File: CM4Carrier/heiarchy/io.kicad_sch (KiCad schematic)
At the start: 3 parts

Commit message: wiring some stuff
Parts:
- added C?: 10u, Capacitor_SMD:C_0805_2012Metric, symbol Device:C
- added D?: (no value), symbol Device:LED
- added R? (x2): (no value), symbol Device:R
- added TP?: (no value), symbol Connector:TestPoint_Flag
- added TP?: (no value), symbol Connector:TestPoint
- added U?: (no value), symbol Power_Management:MIC2025-2YMM
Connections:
- net GND: now also J?.6 (VSS), C?.2, U?.3 (GND)
- net IO_VREF: now also D?.2 (A), R?.2, TP?.1, U?.7 (IN)
- net SD_CMD: now reaches J?.3 (CMD)
- net SD_CMD: now also Module1.62 (SD_CMD)
- net SD_PWR: now reaches J?.4 (VDD)
- net SD_PWR: now also C?.1, U?.6 (OUT), U?.8 (OUT)
- net SD_CLK: now reaches J?.5 (CLK)
- net SD_CLK: now also Module1.57 (SD_CLK)
- net at Module1.21 (PI_nLED_Activity): now also R?.2
- net SD_PWR_ON: now reaches Module1.75 (SD_PWR_ON)
- net SD_PWR_ON: now also R?.1, U?.1 (EN)
- net at Module1.95 (nPI_LED_PWR): now also TP?.1
- new net: D?.1 (K), R?.1
- no-connect marks 0 -> 7
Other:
- note added: "SD CARD"
- note added: "if an sd card is overcurrent... what?"
- moved on the sheet: J?, R?

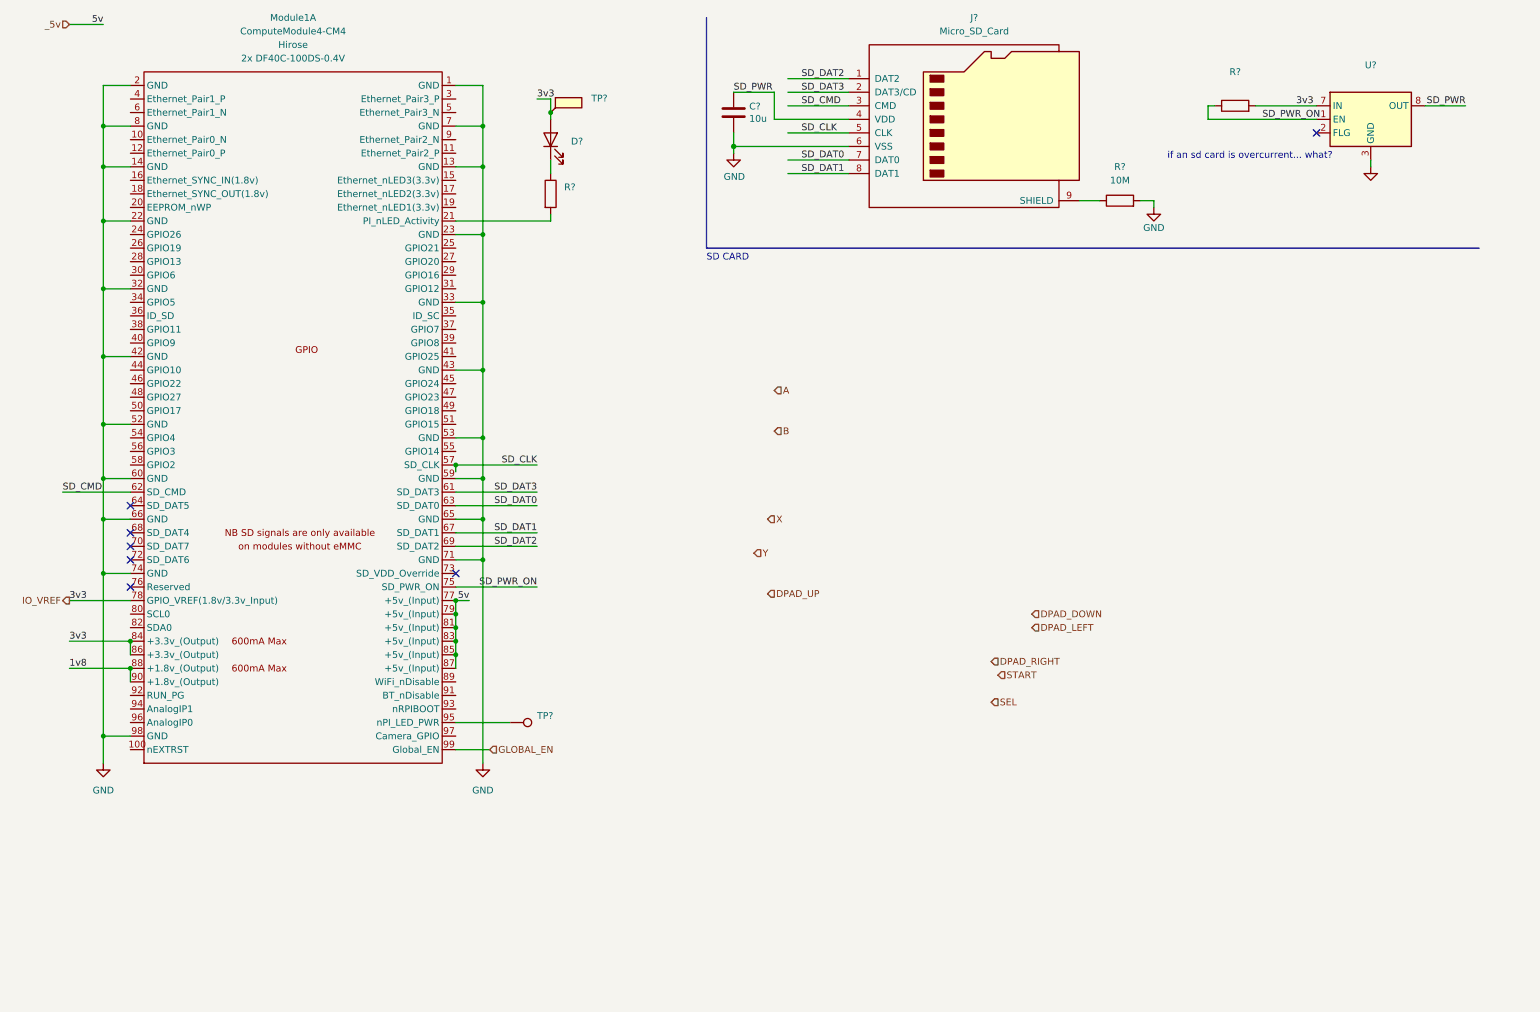
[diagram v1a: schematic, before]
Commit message: footprints  + values
need to do some 3d babeeeeeeeeee
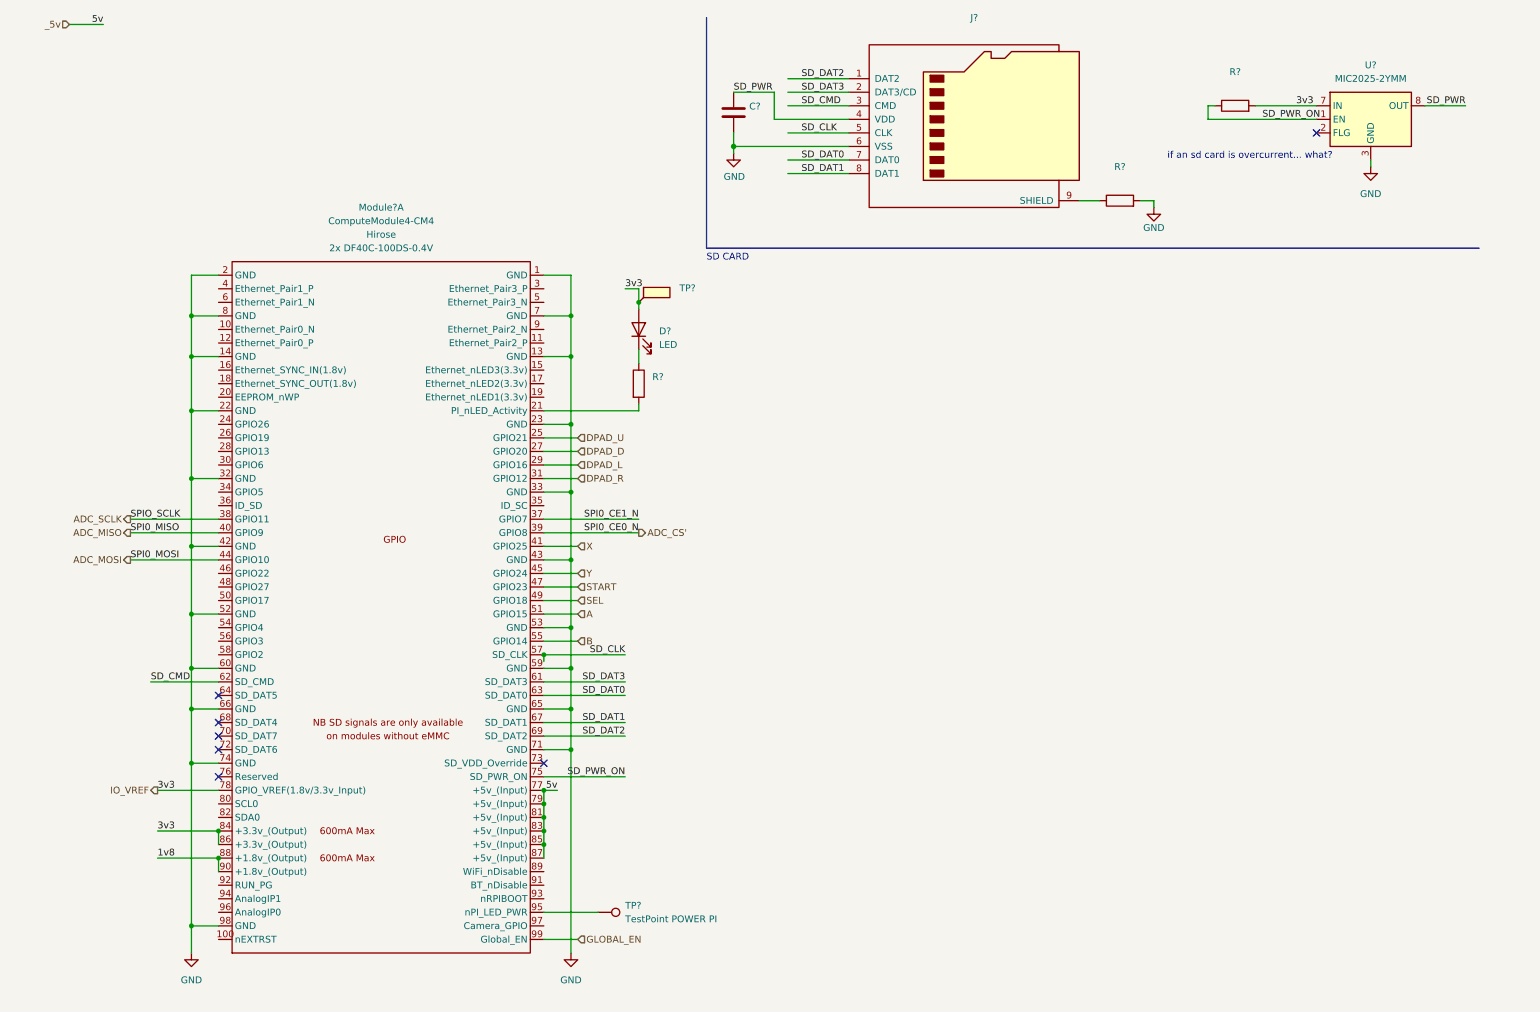
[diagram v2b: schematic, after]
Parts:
- C?: value 10u -> (none); footprint Capacitor_SMD:C_0805_2012Metric -> (none)
- D?: value (none) -> LED
- J?: value Micro_SD_Card -> (none)
- R?: value 10M -> (none)
- TP?: value (none) -> TestPoint POWER PI
- U?: value (none) -> MIC2025-2YMM; footprint (none) -> Package_SO:MSOP-8_3x3mm_P0.65mm
- renumbered Module1 to Module?
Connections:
- net A: now also Module?.51 (GPIO15)
- net B: now also Module?.55 (GPIO14)
- net SEL: now also Module?.49 (GPIO18)
- net START: now also Module?.47 (GPIO23)
- net X: now also Module?.41 (GPIO25)
- net Y: now also Module?.45 (GPIO24)
- net DPAD_U: now reaches Module?.25 (GPIO21)
- net DPAD_D: now reaches Module?.27 (GPIO20)
- net DPAD_L: now reaches Module?.29 (GPIO16)
- net DPAD_R: now reaches Module?.31 (GPIO12)
- net SPI0_CE1_N: now reaches Module?.37 (GPIO7)
- net ADC_SCLK: now reaches Module?.38 (GPIO11)
- net ADC_CS': now reaches Module?.39 (GPIO8)
- net ADC_MISO: now reaches Module?.40 (GPIO9)
- net ADC_MOSI: now reaches Module?.44 (GPIO10)
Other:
- moved on the sheet: D?, Module?A, R?, TP?

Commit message: aa
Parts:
- C?: value (none) -> 10u; footprint (none) -> Capacitor_SMD:C_0805_2012Metric_Pad1.18x1.45mm_HandSolder
- J?: value (none) -> Micro_SD_Card; footprint (none) -> CM4IO:GCT_MEM2067-02-180-00-A_REVB
- R?: value (none) -> nc; footprint (none) -> Resistor_SMD:R_0805_2012Metric_Pad1.20x1.40mm_HandSolder
- R?: value (none) -> 10k; footprint (none) -> Resistor_SMD:R_0805_2012Metric_Pad1.20x1.40mm_HandSolder
- R?: value (none) -> 1k
- TP?: value (none) -> TestPoint_Flag; footprint (none) -> TestPoint:TestPoint_THTPad_1.0x1.0mm_Drill0.5mm
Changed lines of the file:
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@@
       (effects (font (size 1.27 1.27)) (justify left))
     )
-    (property "Value" "" (id 1) (at 132.08 67.1829 0)
-      (effects (font (size 1.27 1.27)) (justify left))
-    )
-    (property "Footprint" "" (id 2) (at 129.54 67.31 0)
+    (property "Value" "TestPoint_Flag" (id 1) (at 132.08 67.1829 0)
+      (effects (font (size 1.27 1.27)) (justify left))
+    )
+    (property "Footprint" "TestPoint:TestPoint_THTPad_1.0x1.0mm_Drill0.5mm" (id 2) (at 129.54 67.31 0)
       (effects (font (size 1.27 1.27)) hide)
     )
@@
     (in_bom yes) (on_board yes) (fields_autoplaced)
     (property "Reference" "R?" (id 0) (at 214.63 41.91 90))
-    (property "Value" "" (id 1) (at 214.63 44.45 90))
-    (property "Footprint" "" (id 2) (at 214.63 50.038 90)
+    (property "Value" "nc" (id 1) (at 214.63 44.45 90))
+    (property "Footprint" "Resistor_SMD:R_0805_2012Metric_Pad1.20x1.40mm_HandSolder" (id 2) (at 214.63 50.038 90)
       (effects (font (size 1.27 1.27)) hide)
     )
@@
     (in_bom yes) (on_board yes) (fields_autoplaced)
     (property "Reference" "R?" (id 0) (at 236.22 24.13 90))
-    (property "Value" "" (id 1) (at 236.22 26.67 90))
-    (property "Footprint" "" (id 2) (at 236.22 32.258 90)
+    (property "Value" "10k" (id 1) (at 236.22 26.67 90))
+    (property "Footprint" "Resistor_SMD:R_0805_2012Metric_Pad1.20x1.40mm_HandSolder" (id 2) (at 236.22 32.258 90)
       (effects (font (size 1.27 1.27)) hide)
     )
@@
     (in_bom yes) (on_board yes) (fields_autoplaced)
     (property "Reference" "J?" (id 0) (at 187.325 13.97 0))
-    (property "Value" "" (id 1) (at 187.325 16.51 0))
-    (property "Footprint" "" (id 2) (at 215.9 25.4 0)
+    (property "Value" "Micro_SD_Card" (id 1) (at 187.325 16.51 0))
+    (property "Footprint" "CM4IO:GCT_MEM2067-02-180-00-A_REVB" (id 2) (at 215.9 25.4 0)
       (effects (font (size 1.27 1.27)) hide)
     )
@@
       (effects (font (size 1.27 1.27)) (justify left))
     )
-    (property "Value" "" (id 1) (at 145.161 32.893 0)
-      (effects (font (size 1.27 1.27)) (justify left))
-    )
-    (property "Footprint" "" (id 2) (at 143.2052 35.56 0)
+    (property "Value" "10u" (id 1) (at 145.161 32.893 0)
+      (effects (font (size 1.27 1.27)) (justify left))
+    )
+    (property "Footprint" "Capacitor_SMD:C_0805_2012Metric_Pad1.18x1.45mm_HandSolder" (id 2) (at 143.2052 35.56 0)
       (effects (font (size 1.27 1.27)) hide)
     )
@@
       (effects (font (size 1.27 1.27)) (justify left))
     )
-    (property "Value" "" (id 1) (at 127 83.8199 0)
-      (effects (font (size 1.27 1.27)) (justify left))
-    )
+    (property "Value" "1k" (id 1) (at 127 83.8199 0)
+      (effects (font (size 1.27 1.27)) (justify left))
+    )

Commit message: pcb next :sunglasses:
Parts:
- gave numbers to parts that had none: 10
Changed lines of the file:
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@@
   (symbol (lib_id "Connector:TestPoint_Flag") (at 124.46 67.31 0) (unit 1)
     (in_bom yes) (on_board yes) (fields_autoplaced)
-    (property "Reference" "TP?" (id 0) (at 132.08 64.6429 0)
+    (property "Reference" "TP2" (id 0) (at 132.08 64.6429 0)
       (effects (font (size 1.27 1.27)) (justify left))
     )
@@
   (symbol (lib_id "Device:R") (at 214.63 48.26 90) (unit 1)
     (in_bom yes) (on_board yes) (fields_autoplaced)
-    (property "Reference" "R?" (id 0) (at 214.63 41.91 90))
+    (property "Reference" "R2" (id 0) (at 214.63 41.91 90))
     (property "Value" "nc" (id 1) (at 214.63 44.45 90))
     (property "Footprint" "Resistor_SMD:R_0805_2012Metric_Pad1.20x1.40mm_HandSolder" (id 2) (at 214.63 50.038 90)
@@
   (symbol (lib_id "power:GND") (at 142.24 39.37 0) (unit 1)
     (in_bom yes) (on_board yes)
-    (property "Reference" "#PWR?" (id 0) (at 142.24 45.72 0)
+    (property "Reference" "#PWR0103" (id 0) (at 142.24 45.72 0)
       (effects (font (size 1.27 1.27)) hide)
     )
@@
   (symbol (lib_id "Device:R") (at 236.22 30.48 90) (unit 1)
     (in_bom yes) (on_board yes) (fields_autoplaced)
-    (property "Reference" "R?" (id 0) (at 236.22 24.13 90))
+    (property "Reference" "R3" (id 0) (at 236.22 24.13 90))
     (property "Value" "10k" (id 1) (at 236.22 26.67 90))
     (property "Footprint" "Resistor_SMD:R_0805_2012Metric_Pad1.20x1.40mm_HandSolder" (id 2) (at 236.22 32.258 90)
@@
   (symbol (lib_id "Connector:Micro_SD_Card") (at 186.69 33.02 0) (unit 1)
     (in_bom yes) (on_board yes) (fields_autoplaced)
-    (property "Reference" "J?" (id 0) (at 187.325 13.97 0))
+    (property "Reference" "J1" (id 0) (at 187.325 13.97 0))
     (property "Value" "Micro_SD_Card" (id 1) (at 187.325 16.51 0))
     (property "Footprint" "CM4IO:GCT_MEM2067-02-180-00-A_REVB" (id 2) (at 215.9 25.4 0)
@@
   (symbol (lib_id "power:GND") (at 261.62 41.91 0) (unit 1)
     (in_bom yes) (on_board yes) (fields_autoplaced)
-    (property "Reference" "#PWR?" (id 0) (at 261.62 48.26 0)
+    (property "Reference" "#PWR0105" (id 0) (at 261.62 48.26 0)
       (effects (font (size 1.27 1.27)) hide)
     )
@@
   (symbol (lib_id "Connector:TestPoint") (at 116.84 181.61 270) (unit 1)
     (in_bom yes) (on_board yes) (fields_autoplaced)
-    (property "Reference" "TP?" (id 0) (at 121.92 180.3399 90)
+    (property "Reference" "TP1" (id 0) (at 121.92 180.3399 90)
       (effects (font (size 1.27 1.27)) (justify left))
     )
@@
   (symbol (lib_id "power:GND") (at 111.76 189.23 0) (unit 1)
     (in_bom yes) (on_board yes) (fields_autoplaced)
-    (property "Reference" "#PWR?" (id 0) (at 111.76 195.58 0)
+    (property "Reference" "#PWR0101" (id 0) (at 111.76 195.58 0)
       (effects (font (size 1.27 1.27)) hide)
     )
@@
   (symbol (lib_id "Device:LED") (at 124.46 72.39 90) (unit 1)
     (in_bom yes) (on_board yes) (fields_autoplaced)
-    (property "Reference" "D?" (id 0) (at 128.27 72.7074 90)
+    (property "Reference" "D1" (id 0) (at 128.27 72.7074 90)
       (effects (font (size 1.27 1.27)) (justify right))
     )
@@
   (symbol (lib_id "power:GND") (at 40.64 189.23 0) (unit 1)
     (in_bom yes) (on_board yes) (fields_autoplaced)
-    (property "Reference" "#PWR?" (id 0) (at 40.64 195.58 0)
+    (property "Reference" "#PWR0102" (id 0) (at 40.64 195.58 0)
       (effects (font (size 1.27 1.27)) hide)
     )
@@
   (symbol (lib_id "Device:C") (at 142.24 31.75 0) (unit 1)
     (in_bom yes) (on_board yes)
-    (property "Reference" "C?" (id 0) (at 145.161 30.5816 0)
+    (property "Reference" "C1" (id 0) (at 145.161 30.5816 0)
       (effects (font (size 1.27 1.27)) (justify left))
     )
@@
   (symbol (lib_id "Power_Management:MIC2025-2YMM") (at 261.62 33.02 0) (unit 1)
     (in_bom yes) (on_board yes) (fields_autoplaced)
-    (property "Reference" "U?" (id 0) (at 261.62 22.86 0))
+    (property "Reference" "U1" (id 0) (at 261.62 22.86 0))
     (property "Value" "MIC2025-2YMM" (id 1) (at 261.62 25.4 0))
     (property "Footprint" "Package_SO:MSOP-8_3x3mm_P0.65mm" (id 2) (at 280.67 39.37 0)
@@
   (symbol (lib_id "Device:R") (at 124.46 82.55 0) (unit 1)
     (in_bom yes) (on_board yes) (fields_autoplaced)
-    (property "Reference" "R?" (id 0) (at 127 81.2799 0)
+    (property "Reference" "R1" (id 0) (at 127 81.2799 0)
       (effects (font (size 1.27 1.27)) (justify left))
     )
@@
   (symbol (lib_id "CM4IO:ComputeModule4-CM4") (at 78.74 118.11 0) (unit 1)
     (in_bom yes) (on_board yes) (fields_autoplaced)
-    (property "Reference" "Module?" (id 0) (at 76.2 49.53 0))
+    (property "Reference" "Module1" (id 0) (at 76.2 49.53 0))
     (property "Value" "ComputeModule4-CM4" (id 1) (at 76.2 52.07 0))
     (property "Footprint" "CM4IO:Raspberry-Pi-4-Compute-Module" (id 2) (at 220.98 144.78 0)
@@
   (symbol (lib_id "power:GND") (at 220.98 49.53 0) (unit 1)
     (in_bom yes) (on_board yes)
-    (property "Reference" "#PWR?" (id 0) (at 220.98 55.88 0)
-      (effects (font (size 1.27 1.27)) hide)
-    )
+    (property "Reference" "#PWR0104" (id 0) (at 220.98 55.88 0)
+      (effects (font (size 1.27 1.27)) hide)
+    )
